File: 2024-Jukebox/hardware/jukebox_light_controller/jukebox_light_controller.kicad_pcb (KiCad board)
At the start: 2 copper layers, 100 x 100 mm, 158 parts, among them J1 HEAD_LEDS, J10 BUTTON_3, J11 BUTTON_4, J12 BUTTON_5, J13 BUTTON_6, J14 BUTTON_7, J15 VOLUME, J16 DISPLAY_1, J17 DISPLAY_2, J2 MOUTH_LEDS, J3 76829-0004, J4 Conn_01x03, J5 ROTARY_SWITCH, J6 BUTTON_1, J7 USB_C_Receptacle_USB2.0, J8 BUTTON_2, J9 RJ45_Wuerth_7499010121A, Q1 2N7002, Q2 2N7002, SW1 SW_DIP_x03, SW2 SW_Push, SW3 SW_Push, U12 W25Q128JVS, U4 AMS1117-3.3, U5 RP2040, U6 W5500, Y1 12MHz, Y2 25MHz

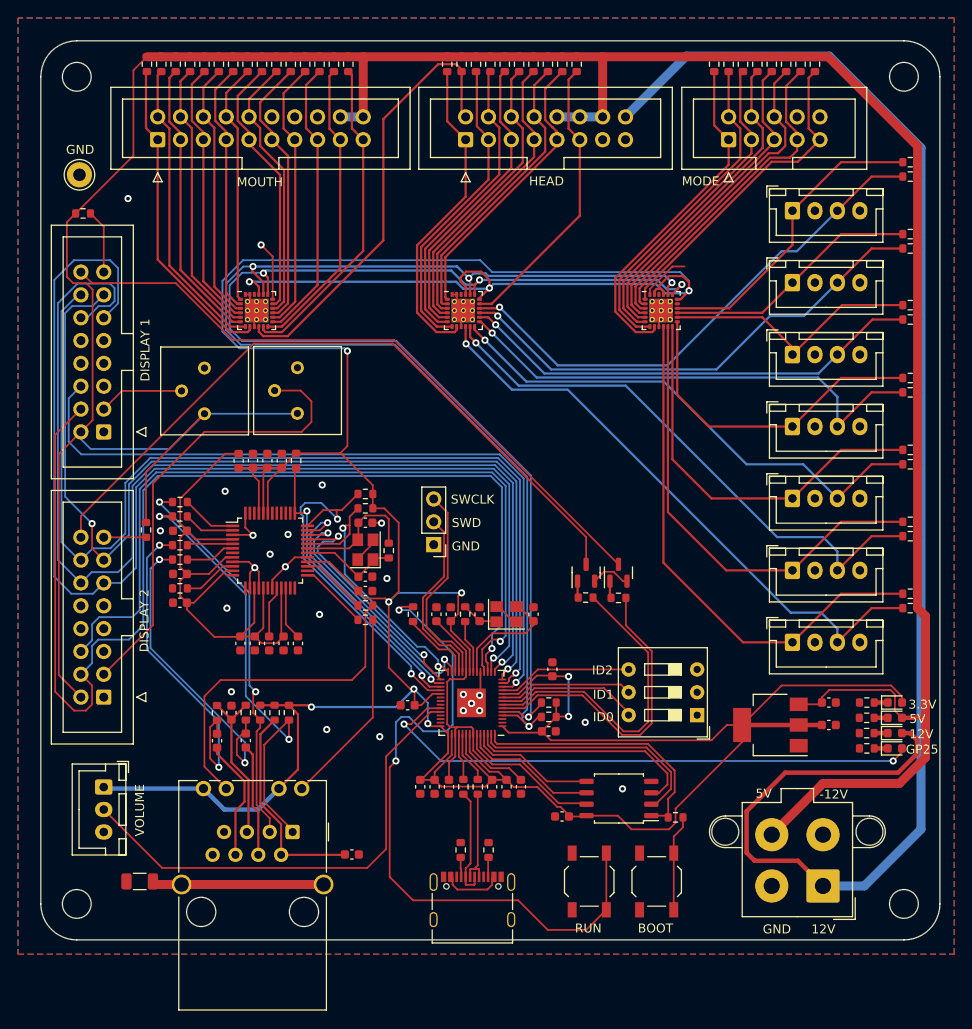
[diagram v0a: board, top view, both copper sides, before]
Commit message: Added level shifters to LCD display signals
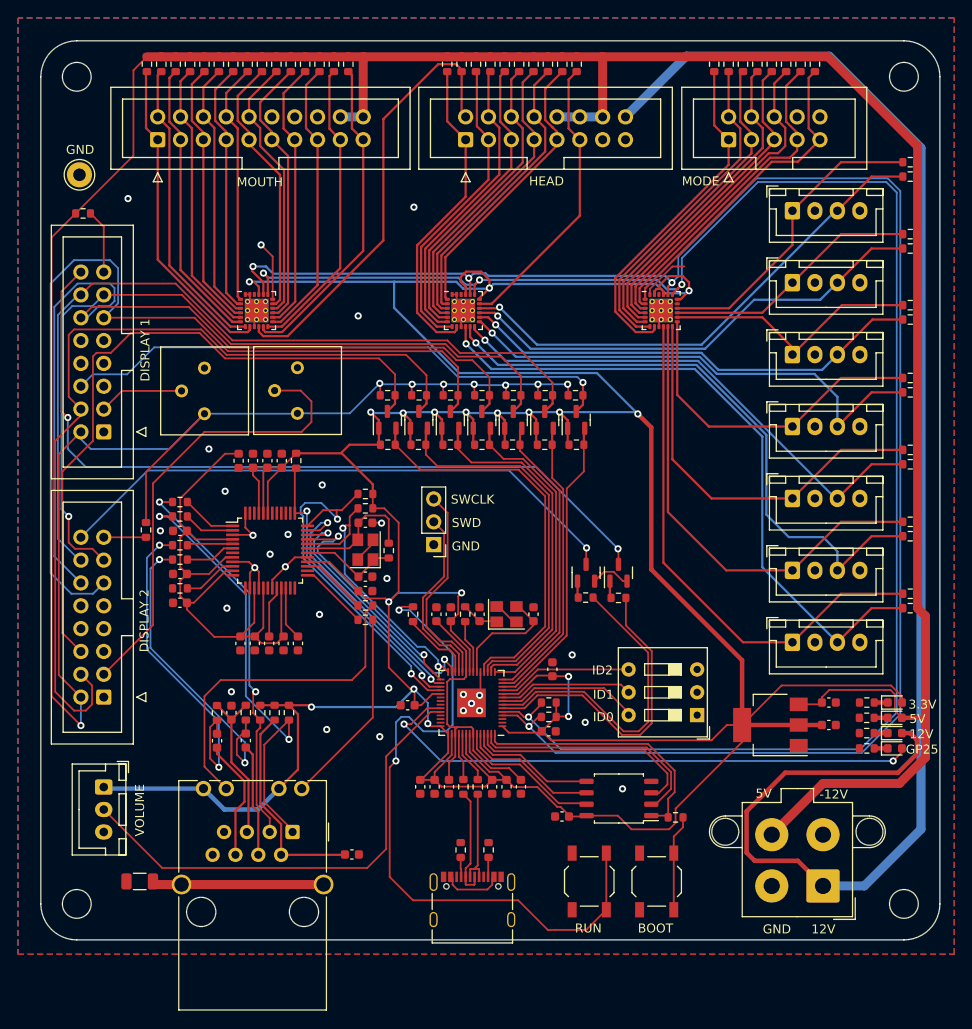
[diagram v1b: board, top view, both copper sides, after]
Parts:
- added Q3: BSS138, Package_TO_SOT_SMD:SOT-23, F.Cu at (56.0, 42.2)
- added Q4: BSS138, Package_TO_SOT_SMD:SOT-23, F.Cu at (52.5, 42.2)
- added Q5: BSS138, Package_TO_SOT_SMD:SOT-23, F.Cu at (49.0, 42.2)
- added Q6: BSS138, Package_TO_SOT_SMD:SOT-23, F.Cu at (45.5, 42.2)
- added Q7: BSS138, Package_TO_SOT_SMD:SOT-23, F.Cu at (42.0, 42.1)
- added Q8: BSS138, Package_TO_SOT_SMD:SOT-23, F.Cu at (59.5, 42.2)
- added Q9: BSS138, Package_TO_SOT_SMD:SOT-23, F.Cu at (38.5, 42.1)
- added R81: 10k, Resistor_SMD:R_0603_1608Metric, F.Cu at (56.0, 44.9)
- added R82: 10k, Resistor_SMD:R_0603_1608Metric, F.Cu at (56.1, 39.4)
- added R83: 10k, Resistor_SMD:R_0603_1608Metric, F.Cu at (52.5, 44.9)
- added R84: 10k, Resistor_SMD:R_0603_1608Metric, F.Cu at (52.6, 39.4)
- added R85: 10k, Resistor_SMD:R_0603_1608Metric, F.Cu at (49.1, 44.9)
- added R86: 10k, Resistor_SMD:R_0603_1608Metric, F.Cu at (49.1, 39.4)
- added R87: 10k, Resistor_SMD:R_0603_1608Metric, F.Cu at (45.5, 44.9)
- added R88: 10k, Resistor_SMD:R_0603_1608Metric, F.Cu at (45.6, 39.4)
- added R89: 10k, Resistor_SMD:R_0603_1608Metric, F.Cu at (42.0, 44.9)
- added R90: 10k, Resistor_SMD:R_0603_1608Metric, F.Cu at (59.6, 44.9)
- added R91: 10k, Resistor_SMD:R_0603_1608Metric, F.Cu at (38.6, 44.9)
- added R92: 10k, Resistor_SMD:R_0603_1608Metric, F.Cu at (42.1, 39.4)
- added R93: 10k, Resistor_SMD:R_0603_1608Metric, F.Cu at (59.5, 39.4)
- added R94: 10k, Resistor_SMD:R_0603_1608Metric, F.Cu at (38.6, 39.4)
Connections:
- U5 pad 12: LCD_E1 -> LCD_E1_LO
- U5 pad 13: DB7 -> DB7_LO
- U5 pad 14: DB6 -> DB6_LO
- U5 pad 15: DB5 -> DB5_LO
- U5 pad 16: DB4 -> DB4_LO
- U5 pad 17: LCD_RS -> LCD_RS_LO
- U5 pad 18: LCD_E2 -> LCD_E2_LO
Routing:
- net +5V: track 339.6 -> 414.2 mm, vias 0 -> 8
- net SDA: track 137.6 -> 194.7 mm
- net SCL: track 135.9 -> 192.1 mm
- net +3.3V: track 456.2 -> 506.2 mm, vias 11 -> 18
- net LCD_E2_LO: track 0.00 -> 44.8 mm
- net LCD_RS_LO: track 0.00 -> 42.6 mm
- net DB4_LO: track 0.00 -> 39.1 mm
- net DB5_LO: track 0.00 -> 35.6 mm
- net LCD_E1_LO: track 0.00 -> 33.4 mm
- net DB6_LO: track 0.00 -> 33.1 mm
- net DB7_LO: track 0.00 -> 32.5 mm
- net LCD_RS: track 129.5 -> 97.1 mm, vias 1 -> 0
- net DB4: track 132.6 -> 101.6 mm, vias 1 -> 0
- net DB5: track 126.6 -> 99.2 mm, vias 1 -> 0
- net DB6: track 111.8 -> 90.3 mm, vias 2 -> 1
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
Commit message: Updated schematic
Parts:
- removed Q2: 2N7002, Package_TO_SOT_SMD:SOT-23
- added Q10: MMBT2222, Package_TO_SOT_SMD:SOT-23, F.Cu at (60.6, 59.1)
- Q1: value 2N7002 -> MMBT2222
- R79, R80: value 100 -> 470
- moved Q1 0.06 mm to (64.2, 59.1)

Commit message: Minor fixes
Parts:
- R53, R55, R56, R57, R58, R59: value 5.1k -> 1k
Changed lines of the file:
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@@
         (effects (font (size 1 1) (thickness 0.15)))
     )
-    (fp_text value "5.1k" (at 0 1.43) (layer "F.Fab")
+    (fp_text value "1k" (at 0 1.43) (layer "F.Fab")
         (effects (font (size 1 1) (thickness 0.15)))
     )
@@
         (effects (font (size 1 1) (thickness 0.15)))
     )
-    (fp_text value "5.1k" (at 0 1.43) (layer "F.Fab")
+    (fp_text value "1k" (at 0 1.43) (layer "F.Fab")
         (effects (font (size 1 1) (thickness 0.15)))
     )
@@
         (effects (font (size 1 1) (thickness 0.15)))
     )
-    (fp_text value "5.1k" (at 0 1.43) (layer "F.Fab")
+    (fp_text value "1k" (at 0 1.43) (layer "F.Fab")
         (effects (font (size 1 1) (thickness 0.15)))
     )
@@
         (effects (font (size 1 1) (thickness 0.15)))
     )
-    (fp_text value "5.1k" (at 0 1.43) (layer "F.Fab")
+    (fp_text value "1k" (at 0 1.43) (layer "F.Fab")
         (effects (font (size 1 1) (thickness 0.15)))
     )
@@
         (effects (font (size 1 1) (thickness 0.15)))
     )
-    (fp_text value "5.1k" (at 0 1.43) (layer "F.Fab")
+    (fp_text value "1k" (at 0 1.43) (layer "F.Fab")
         (effects (font (size 1 1) (thickness 0.15)))
     )
@@
         (effects (font (size 1 1) (thickness 0.15)))
     )
-    (fp_text value "5.1k" (at 0 1.43) (layer "F.Fab")
+    (fp_text value "1k" (at 0 1.43) (layer "F.Fab")
         (effects (font (size 1 1) (thickness 0.15)))
     )

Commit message: Updated pullup resistor values
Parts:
- R53, R55, R56, R57, R58, R59: value 1k -> 100
- R54: value 5.1k -> 100
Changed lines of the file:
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@@
         (effects (font (size 1 1) (thickness 0.15)))
     )
-    (fp_text value "1k" (at 0 1.43) (layer "F.Fab")
+    (fp_text value "100" (at 0 1.43) (layer "F.Fab")
         (effects (font (size 1 1) (thickness 0.15)))
     )
@@
         (effects (font (size 1 1) (thickness 0.15)))
     )
-    (fp_text value "1k" (at 0 1.43) (layer "F.Fab")
+    (fp_text value "100" (at 0 1.43) (layer "F.Fab")
         (effects (font (size 1 1) (thickness 0.15)))
     )
@@
         (effects (font (size 1 1) (thickness 0.15)))
     )
-    (fp_text value "5.1k" (at 0 1.43) (layer "F.Fab")
+    (fp_text value "100" (at 0 1.43) (layer "F.Fab")
         (effects (font (size 1 1) (thickness 0.15)))
     )
@@
         (effects (font (size 1 1) (thickness 0.15)))
     )
-    (fp_text value "1k" (at 0 1.43) (layer "F.Fab")
+    (fp_text value "100" (at 0 1.43) (layer "F.Fab")
         (effects (font (size 1 1) (thickness 0.15)))
     )
@@
         (effects (font (size 1 1) (thickness 0.15)))
     )
-    (fp_text value "1k" (at 0 1.43) (layer "F.Fab")
+    (fp_text value "100" (at 0 1.43) (layer "F.Fab")
         (effects (font (size 1 1) (thickness 0.15)))
     )
@@
         (effects (font (size 1 1) (thickness 0.15)))
     )
-    (fp_text value "1k" (at 0 1.43) (layer "F.Fab")
+    (fp_text value "100" (at 0 1.43) (layer "F.Fab")
         (effects (font (size 1 1) (thickness 0.15)))
     )
@@
         (effects (font (size 1 1) (thickness 0.15)))
     )
-    (fp_text value "1k" (at 0 1.43) (layer "F.Fab")
+    (fp_text value "100" (at 0 1.43) (layer "F.Fab")
         (effects (font (size 1 1) (thickness 0.15)))
     )
